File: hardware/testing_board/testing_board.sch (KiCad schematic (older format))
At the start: 40 parts

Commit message: updates to training board
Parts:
- added D? (x4): LED, symbol Device:LED
- added J?: B4B-XH-A_LF__SN_, digikey-footprints:PinHeader_1x4_P2.5mm_Drill1.1mm, symbol dk_Rectangular-Connectors-Headers-Male-Pins:B4B-XH-A_LF__SN_
- added R? (x4): R_Small, symbol Device:R_Small
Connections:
- net GND: now also D?.1 (K), D?.1 (K), D?.1 (K), D?.1 (K)
- new net: J?.1, R?.2
- new net: J?.2, R?.2
- new net: J?.3, R?.2
- new net: J?.4, R?.2
- new net: D?.2 (A), R?.1 (x4)
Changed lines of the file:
@@
 Wire Notes Line
 	5500 2200 5500 1100
+$Comp
+L dk_Rectangular-Connectors-Headers-Male-Pins:B4B-XH-A_LF__SN_ J?
+U 1 1 6164C117
+P 6050 5750
+F 0 "J?" V 5825 5758 50  0000 C CNN
+F 1 "B4B-XH-A_LF__SN_" V 5916 5758 50  0000 C CNN
+F 2 "digikey-footprints:PinHeader_1x4_P2.5mm_Drill1.1mm" H 6250 5950 60  0001 L CNN
+F 3 "http://www.jst-mfg.com/product/pdf/eng/eXH.pdf" H 6250 6050 60  0001 L CNN
+F 4 "455-2249-ND" H 6250 6150 60  0001 L CNN "Digi-Key_PN"
+F 5 "B4B-XH-A(LF)(SN)" H 6250 6250 60  0001 L CNN "MPN"
+F 6 "Connectors, Interconnects" H 6250 6350 60  0001 L CNN "Category"
+F 7 "Rectangular Connectors - Headers, Male Pins" H 6250 6450 60  0001 L CNN "Family"
+F 8 "http://www.jst-mfg.com/product/pdf/eng/eXH.pdf" H 6250 6550 60  0001 L CNN "DK_Datasheet_Link"
+F 9 "/product-detail/en/jst-sales-america-inc/B4B-XH-A(LF)(SN)/455-2249-ND/1651047" H 6250 6650 60  0001 L CNN "DK_Detail_Page"
+F 10 "CONN HEADER VERT 4POS 2.5MM" H 6250 6750 60  0001 L CNN "Description"
+F 11 "JST Sales America Inc." H 6250 6850 60  0001 L CNN "Manufacturer"
+F 12 "Active" H 6250 6950 60  0001 L CNN "Status"
+	1    6050 5750
+	0    1    1    0
+$EndComp
+$Comp
+L Device:R_Small R?
+U 1 1 6164C11F
+P 6400 5850
+F 0 "R?" V 6204 5850 50  0000 C CNN
+F 1 "R_Small" V 6295 5850 50  0000 C CNN
+F 2 "" H 6400 5850 50  0001 C CNN
+F 3 "~" H 6400 5850 50  0001 C CNN
+	1    6400 5850
+	0    1    1    0
+$EndComp
+$Comp
+L Device:R_Small R?
+U 1 1 6164C125
+P 6400 5550
+F 0 "R?" V 6204 5550 50  0000 C CNN
+F 1 "R_Small" V 6295 5550 50  0000 C CNN
+F 2 "" H 6400 5550 50  0001 C CNN
+F 3 "~" H 6400 5550 50  0001 C CNN
+	1    6400 5550
+	0    1    1    0
+$EndComp
+$Comp
+L Device:LED D?
+U 1 1 6164C12B
+P 6800 5850
+F 0 "D?" H 6793 5595 50  0000 C CNN
+F 1 "LED" H 6793 5686 50  0000 C CNN
+F 2 "" H 6800 5850 50  0001 C CNN
+F 3 "~" H 6800 5850 50  0001 C CNN
+	1    6800 5850
+	-1   0    0    1
+$EndComp
+$Comp
+L Device:LED D?
+U 1 1 6164C131
+P 6800 5550
+F 0 "D?" H 6793 5295 50  0000 C CNN
+F 1 "LED" H 6793 5386 50  0000 C CNN
+F 2 "" H 6800 5550 50  0001 C CNN
+F 3 "~" H 6800 5550 50  0001 C CNN
+	1    6800 5550
+	-1   0    0    1
+$EndComp
+Wire Wire Line
+	6150 5750 6150 5550
+Wire Wire Line
+	6150 5550 6300 5550
+Wire Wire Line
+	6500 5550 6650 5550
+Wire Wire Line
+	6150 5850 6300 5850
+Wire Wire Line
+	6500 5850 6650 5850
+$Comp
+L power:GND #PWR?
+U 1 1 6164C13C
+P 7200 5700
+F 0 "#PWR?" H 7200 5450 50  0001 C CNN
+F 1 "GND" V 7205 5572 50  0000 R CNN
+F 2 "" H 7200 5700 50  0001 C CNN
+F 3 "" H 7200 5700 50  0001 C CNN
+	1    7200 5700
+	0    -1   -1   0
+$EndComp
+Wire Wire Line
+	6950 5550 7200 5550
+Wire Wire Line
+	7200 5550 7200 5700
+Wire Wire Line
+	6950 5850 7200 5850
+Wire Wire Line
+	7200 5850 7200 5700
+Connection ~ 7200 5700
+$Comp
+L Device:R_Small R?
+U 1 1 61668427
+P 6400 5950
+F 0 "R?" V 6204 5950 50  0000 C CNN
+F 1 "R_Small" V 6295 5950 50  0000 C CNN
+F 2 "" H 6400 5950 50  0001 C CNN
+F 3 "~" H 6400 5950 50  0001 C CNN
+	1    6400 5950
+	0    1    1    0
+$EndComp
+$Comp
+L Device:R_Small R?
+U 1 1 616689D9
+P 6400 6100
+F 0 "R?" V 6204 6100 50  0000 C CNN
+F 1 "R_Small" V 6295 6100 50  0000 C CNN
+F 2 "" H 6400 6100 50  0001 C CNN
+F 3 "~" H 6400 6100 50  0001 C CNN
+	1    6400 6100
+	0    1    1    0
+$EndComp
+$Comp
+L Device:LED D?
+U 1 1 61668C6A
+P 6800 6000
+F 0 "D?" H 6793 5745 50  0000 C CNN
+F 1 "LED" H 6793 5836 50  0000 C CNN
+F 2 "" H 6800 6000 50  0001 C CNN
+F 3 "~" H 6800 6000 50  0001 C CNN
+	1    6800 6000
+	-1   0    0    1
+$EndComp
+$Comp
+L Device:LED D?
+U 1 1 6166925E
+P 6800 6150
+F 0 "D?" H 6793 5895 50  0000 C CNN
+F 1 "LED" H 6793 5986 50  0000 C CNN
+F 2 "" H 6800 6150 50  0001 C CNN
+F 3 "~" H 6800 6150 50  0001 C CNN
+	1    6800 6150
+	-1   0    0    1
+$EndComp
+Wire Wire Line
+	6150 5950 6300 5950
+Wire Wire Line
+	6150 6050 6150 6100
+Wire Wire Line
+	6150 6100 6300 6100
+Wire Wire Line
+	6500 5950 6650 5950
+Wire Wire Line
+	6650 5950 6650 6000
+Wire Wire Line
+	6500 6100 6650 6100
+Wire Wire Line
+	6650 6100 6650 6150
+Wire Wire Line
+	6950 6000 7200 6000
+Wire Wire Line
+	7200 6000 7200 5850
+Connection ~ 7200 5850
+Wire Wire Line
+	6950 6150 7200 6150
+Wire Wire Line
+	7200 6150 7200 6000
+Connection ~ 7200 6000
+Wire Notes Line
+	5550 5250 7550 5250
+Wire Notes Line
+	7550 5250 7550 6350
+Wire Notes Line
+	7550 6350 5550 6350
+Wire Notes Line
+	5550 6350 5550 5250
 $EndSCHEMATC

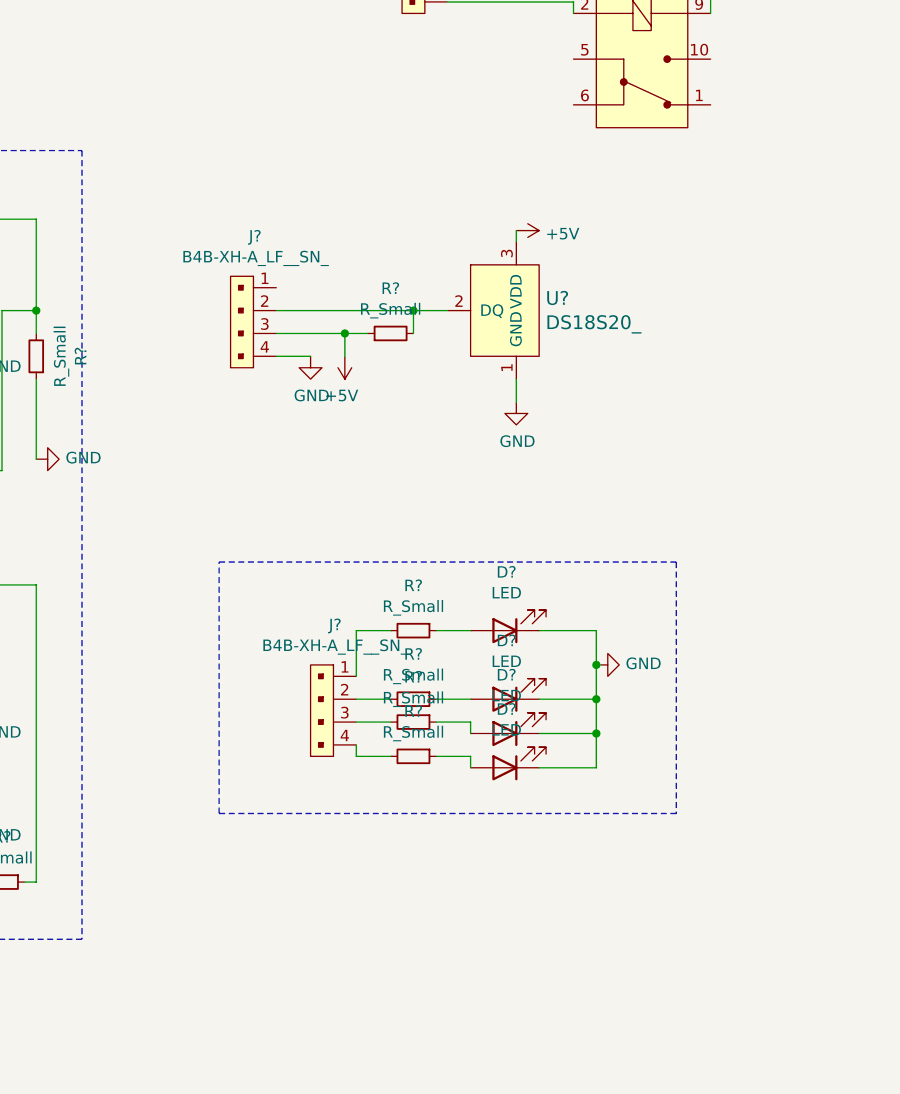
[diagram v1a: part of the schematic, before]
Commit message: update testing board, and add media for documentation
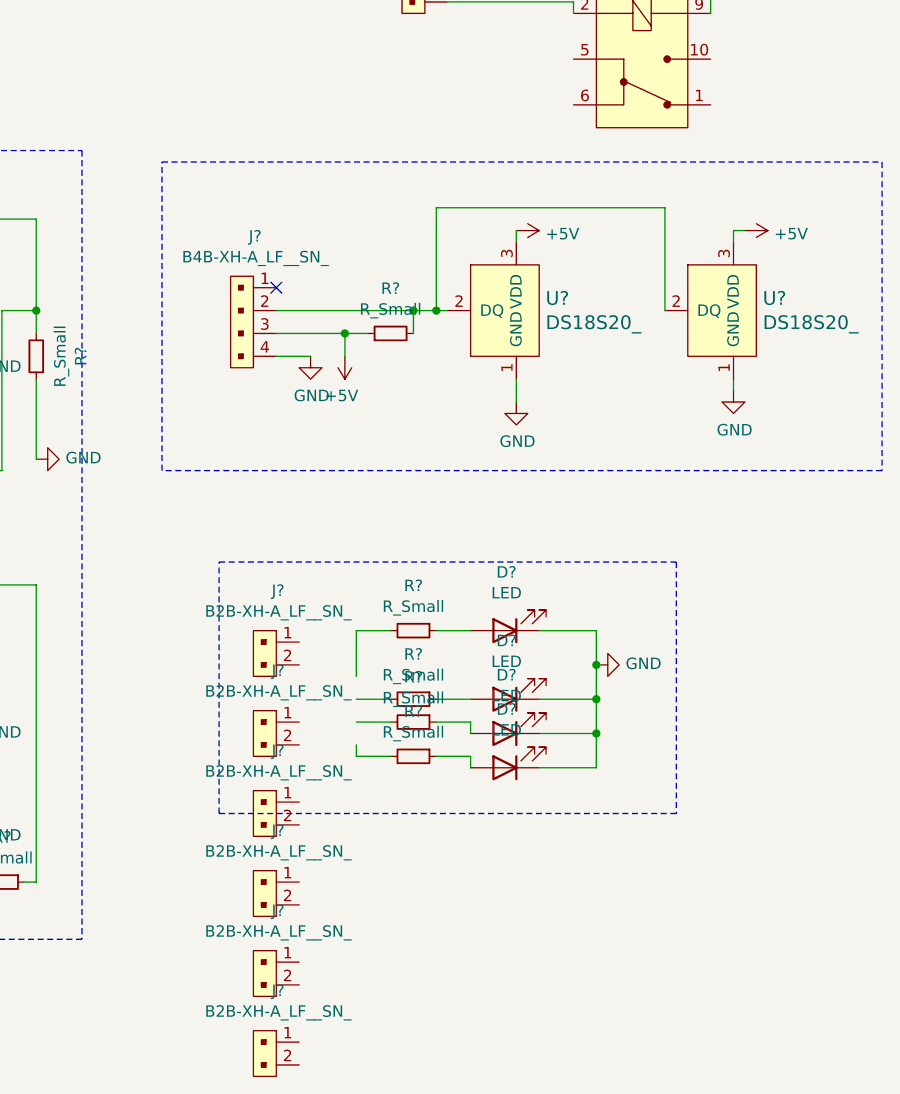
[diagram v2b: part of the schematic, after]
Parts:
- removed J?: B4B-XH-A_LF__SN_, digikey-footprints:PinHeader_1x4_P2.5mm_Drill1.1mm, symbol dk_Rectangular-Connectors-Headers-Male-Pins:B4B-XH-A_LF__SN_
- added J? (x6): B2B-XH-A_LF__SN_, digikey-footprints:PinHeader_1x2_P2.5mm_Drill1.1mm, symbol dk_Rectangular-Connectors-Headers-Male-Pins:B2B-XH-A_LF__SN_
- added U?: DS18S20_, digikey-footprints:TO-92-3, symbol dk_Temperature-Sensors-Analog-and-Digital-Output:DS18S20_
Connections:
- wire segments 118 -> 125
- no-connect marks 0 -> 1
